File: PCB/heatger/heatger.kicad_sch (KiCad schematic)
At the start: 22 parts, among them J1 RPI, J2 DC command, J3 AC Pilote, J4 USB_B_Micro, U1 TLP3023, U2 TLP3023, U3 TLP3023, U4 TLP3023, U5 P82B715DR

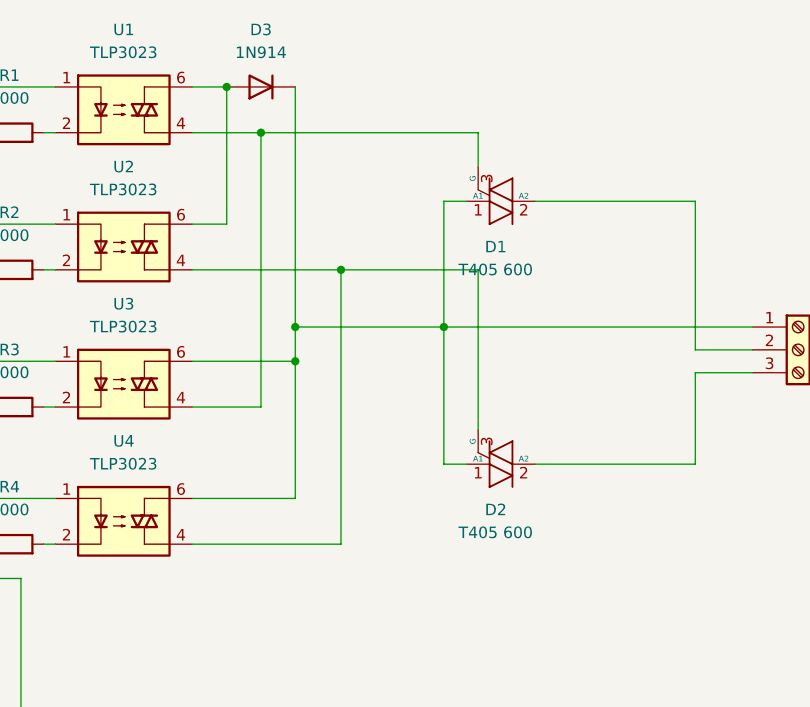
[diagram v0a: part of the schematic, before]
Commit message: invert wiring for pin headers
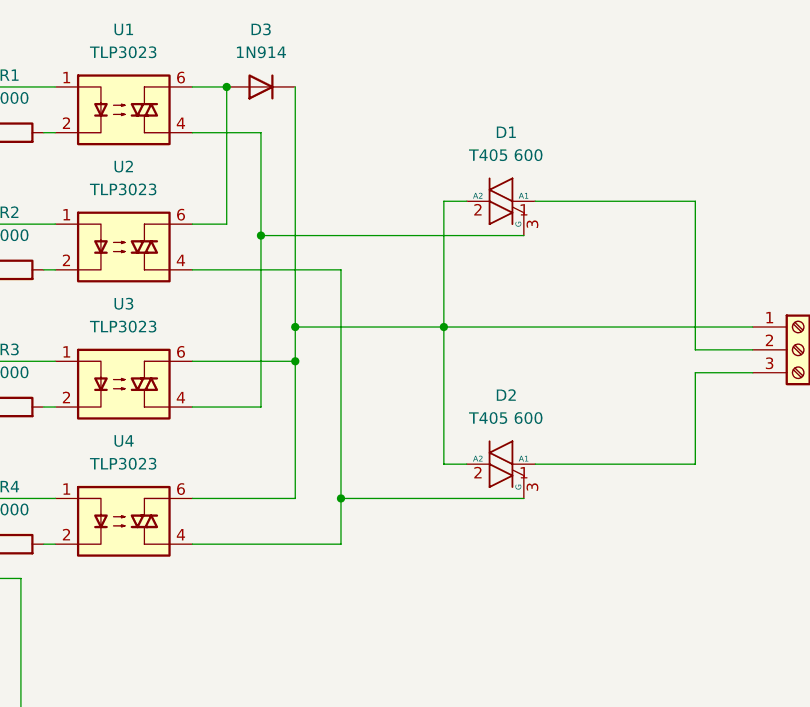
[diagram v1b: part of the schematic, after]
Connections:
- net at D3.1 (K), J3.1 (Pin_1), U3.6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: now also D1.2 (A2), D2.2 (A2); no longer D1.1 (A1), D2.1 (A1)
- net at J3.2 (Pin_2): now also D1.1 (A1); no longer D1.2 (A2)
- net at J3.3 (Pin_3): now also D2.1 (A1); no longer D2.2 (A2)
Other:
- moved on the sheet: D1, D2
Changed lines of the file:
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@@
   (junction (at 97.79 142.24) (diameter 0) (color 0 0 0 0)
   )
-  (junction (at 199.39 60.96) (diameter 0) (color 0 0 0 0)
-  )
   (junction (at 194.31 67.31) (diameter 0) (color 0 0 0 0)
   )
@@
   (junction (at 119.38 111.76) (diameter 0) (color 0 0 0 0)
   )
-  (junction (at 190.5 45.72) (diameter 0) (color 0 0 0 0)
-  )
   (junction (at 116.84 111.76) (diameter 0) (color 0 0 0 0)
   )
   (junction (at 105.41 111.76) (diameter 0) (color 0 0 0 0)
+  )
+  (junction (at 199.39 86.36) (diameter 0) (color 0 0 0 0)
+  )
+  (junction (at 190.5 57.15) (diameter 0) (color 0 0 0 0)
   )
   (junction (at 97.79 113.03) (diameter 0) (color 0 0 0 0)
@@
     (stroke (width 0) (type default))
   )
-  (wire (pts (xy 214.63 78.74) (xy 214.63 60.96))
-    (stroke (width 0) (type default))
-  )
   (wire (pts (xy 97.79 92.71) (xy 97.79 69.85))
     (stroke (width 0) (type default))
@@
     (stroke (width 0) (type default))
   )
-  (wire (pts (xy 190.5 76.2) (xy 190.5 45.72))
+  (wire (pts (xy 190.5 76.2) (xy 190.5 57.15))
     (stroke (width 0) (type default))
   )
@@
     (stroke (width 0) (type default))
   )
-  (wire (pts (xy 214.63 45.72) (xy 214.63 49.53))
-    (stroke (width 0) (type default))
-  )
   (wire (pts (xy 119.38 111.76) (xy 147.32 111.76))
     (stroke (width 0) (type default))
@@
     (stroke (width 0) (type default))
   )
+  (wire (pts (xy 199.39 86.36) (xy 199.39 60.96))
+    (stroke (width 0) (type default))
+  )
   (wire (pts (xy 114.3 110.49) (xy 114.3 146.05))
     (stroke (width 0) (type default))
@@
     (stroke (width 0) (type default))
   )
-  (wire (pts (xy 190.5 45.72) (xy 214.63 45.72))
-    (stroke (width 0) (type default))
-  )
   (wire (pts (xy 31.75 142.24) (xy 31.75 52.07))
     (stroke (width 0) (type default))
   )
+  (wire (pts (xy 190.5 57.15) (xy 190.5 45.72))
+    (stroke (width 0) (type default))
+  )
   (wire (pts (xy 158.75 95.25) (xy 158.75 91.44))
     (stroke (width 0) (type default))
@@
     (stroke (width 0) (type default))
   )
-  (wire (pts (xy 199.39 60.96) (xy 214.63 60.96))
-    (stroke (width 0) (type default))
-  )
   (wire (pts (xy 119.38 143.51) (xy 119.38 146.05))
     (stroke (width 0) (type default))
@@
     (stroke (width 0) (type default))
   )
-  (wire (pts (xy 199.39 91.44) (xy 199.39 60.96))
+  (wire (pts (xy 199.39 91.44) (xy 199.39 86.36))
     (stroke (width 0) (type default))
   )
@@
     (stroke (width 0) (type default))
   )
+  (wire (pts (xy 199.39 86.36) (xy 219.71 86.36))
+    (stroke (width 0) (type default))
+  )
   (wire (pts (xy 147.32 111.76) (xy 147.32 133.35))
     (stroke (width 0) (type default))
@@
   )
   (wire (pts (xy 97.79 142.24) (xy 31.75 142.24))
+    (stroke (width 0) (type default))
+  )
+  (wire (pts (xy 190.5 57.15) (xy 219.71 57.15))
     (stroke (width 0) (type default))
   )
@@
     )
   )
-  (symbol (lib_id "Device:Q_TRIAC_A1A2G") (at 217.17 53.34 270) (unit 1)
-    (in_bom yes) (on_board yes) (dnp no) (fields_autoplaced)
-    (property "Reference" "D1" (at 216.5858 58.42 90)
-      (effects (font (size 1.27 1.27)))
-    )
-    (property "Value" "T405 600" (at 216.5858 60.96 90)
-      (effects (font (size 1.27 1.27)))
-    )
-    (property "Footprint" "VREG_L78M08CDT-TR:VREG_L78M08CDT-TR" (at 217.805 55.245 90)
+  (symbol (lib_id "Device:Q_TRIAC_A1A2G") (at 217.17 53.34 90) (unit 1)
+    (in_bom yes) (on_board yes) (dnp no) (fields_autoplaced)
+    (property "Reference" "D1" (at 217.7542 45.72 90)
+      (effects (font (size 1.27 1.27)))
+    )
+    (property "Value" "T405 600" (at 217.7542 48.26 90)
+      (effects (font (size 1.27 1.27)))
+    )
+    (property "Footprint" "VREG_L78M08CDT-TR:VREG_L78M08CDT-TR" (at 216.535 51.435 90)
       (effects (font (size 1.27 1.27)) hide)
     )
@@
     )
   )
-  (symbol (lib_id "Device:Q_TRIAC_A1A2G") (at 217.17 82.55 270) (unit 1)
-    (in_bom yes) (on_board yes) (dnp no) (fields_autoplaced)
-    (property "Reference" "D2" (at 216.5858 87.63 90)
-      (effects (font (size 1.27 1.27)))
-    )
-    (property "Value" "T405 600" (at 216.5858 90.17 90)
-      (effects (font (size 1.27 1.27)))
-    )
-    (property "Footprint" "VREG_L78M08CDT-TR:VREG_L78M08CDT-TR" (at 217.805 84.455 90)
-      (effects (font (size 1.27 1.27)) hide)
-    )
+  (symbol (lib_id "Device:Q_TRIAC_A1A2G") (at 217.17 82.55 90) (unit 1)
+    (in_bom yes) (on_board yes) (dnp no) (fields_autoplaced)
+    (property "Reference" "D2" (at 217.7542 74.93 90)
+      (effects (font (size 1.27 1.27)))
+    )
+    (property "Value" "T405 600" (at 217.7542 77.47 90)
+      (effects (font (size 1.27 1.27)))
+    )
+    (property "Footprint" "VREG_L78M08CDT-TR:VREG_L78M08CDT-TR" (at 216.535 80.645 90)
+      (effects (font (size 1.27 1.27)) hide)
+    )
